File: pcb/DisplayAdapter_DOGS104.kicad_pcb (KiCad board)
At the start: 2 copper layers, 39 x 30 mm, 12 parts, among them J1 Conn_01x07_Male, U1 EA_DOGS104x-A

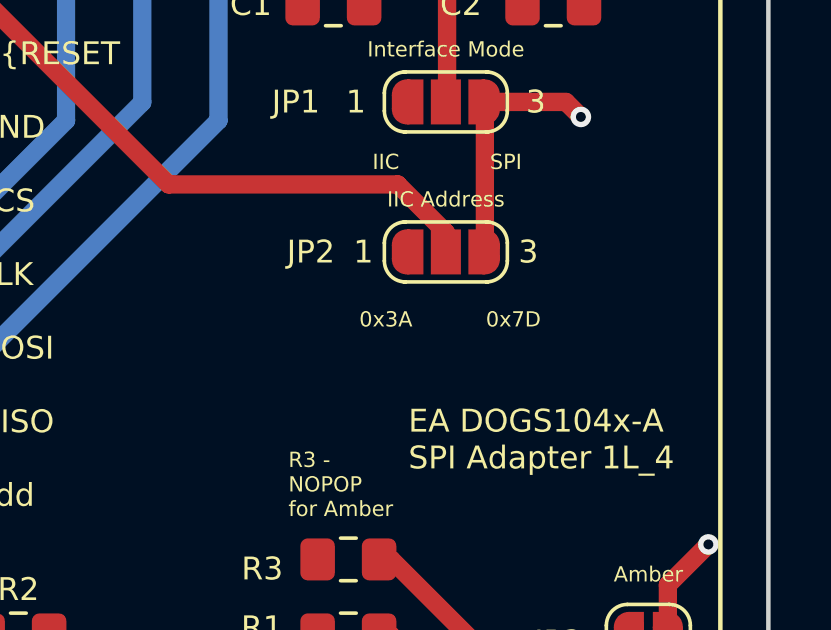
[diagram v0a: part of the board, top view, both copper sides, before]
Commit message: Correction to the IIC address
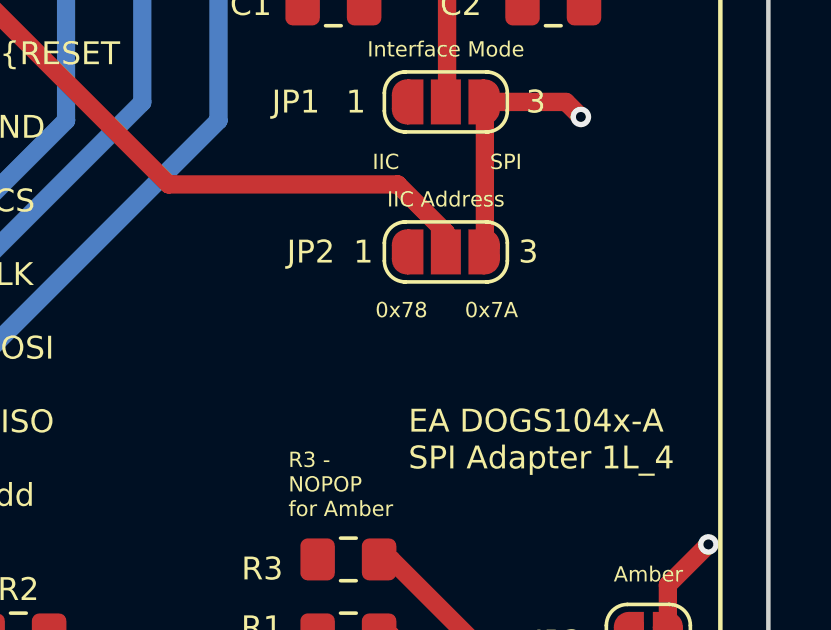
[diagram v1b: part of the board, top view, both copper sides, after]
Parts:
- moved REF** 2.54 mm to (163.1, 95.0)
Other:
- board text added: "0x78"
- board text added: "0x7A"
- board text removed: "0x3A"
- board text removed: "0x7D"
